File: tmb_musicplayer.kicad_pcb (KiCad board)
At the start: 2 copper layers, 99.1 x 95.3 mm, 138 parts, among them J1 Micro_SD, J2 RC522_Header, J3 Screw_Terminal_1x02, P1 SWD, P2 VolDown, P3 Prev, P4 Play, P5 Next, P6 VolUp, P7 CONN_02X10, Q1 BSS138, U1 VS1053, U2 STM32F407VGTx_minimal, U3 LD3985M18R, U4 LM22676QMRX-5.0, U5 LD3985M33R, U7 STEREO-AUDIO-JACK, Y1 12.288 Mhz, Y2 8MHz

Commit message: new layout
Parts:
- removed JP1, JP2: JUMPER, Capacitors_SMD:C_0603
- added C56: 1uF, Capacitors_SMD:C_0603, F.Cu at (64.4, 154.1)
- added C57: 100nF, Capacitors_SMD:C_0402, F.Cu at (62.5, 159.9)
- added C58: 10nF, Capacitors_SMD:C_0603, F.Cu at (66.4, 160.5)
- added C59: 1uF, Capacitors_SMD:C_0603, F.Cu at (68.8, 152.9)
- added C60: 100nF, Capacitors_SMD:C_0402, F.Cu at (78.4, 156.0)
- added R46: 0, Resistors_SMD:R_0603, F.Cu at (77.7, 159.9)
- added R47: 0, Resistors_SMD:R_0603, F.Cu at (73.9, 161.1)
- added R48: 0, Resistors_SMD:R_0603, F.Cu at (70.4, 160.5)
- added R49: 0, Resistors_SMD:R_0603, F.Cu at (75.2, 153.5)
- added U6: LD3985M33R, TO_SOT_Packages_SMD:SOT-23-5, F.Cu at (156.4, 144.0)
- added W10: SCLK, Measurement_Points:Measurement_Point_Round-SMD-Pad_Small, F.Cu at (70.7, 172.6)
- added W11: MCLK, Measurement_Points:Measurement_Point_Round-SMD-Pad_Small, F.Cu at (118.3, 167.5)
- added W12: XRESET, Measurement_Points:Measurement_Point_Round-SMD-Pad_Small, F.Cu at (129.1, 167.5)
- added W13: LROUT, Measurement_Points:Measurement_Point_Round-SMD-Pad_Small, F.Cu at (145.0, 169.4)
- added W14: LEDDIN, Measurement_Points:Measurement_Point_Round-SMD-Pad_Small, F.Cu at (97.4, 172.6)
- added W15: BTNDO, Measurement_Points:Measurement_Point_Round-SMD-Pad_Small, F.Cu at (134.8, 169.4)
- added W16: SDA, Measurement_Points:Measurement_Point_Round-SMD-Pad_Small, F.Cu at (155.2, 169.4)
- added W17: RESET, Measurement_Points:Measurement_Point_Round-SMD-Pad_Small, F.Cu at (77.7, 174.5)
- added W18: SCK, Measurement_Points:Measurement_Point_Round-SMD-Pad_Small, F.Cu at (91.7, 173.2)
- added W19: IRQ, Measurement_Points:Measurement_Point_Round-SMD-Pad_Small, F.Cu at (61.2, 172.6)
- added W20: MOSI, Measurement_Points:Measurement_Point_Round-SMD-Pad_Small, F.Cu at (50.4, 166.2)
- added W21: MISO, Measurement_Points:Measurement_Point_Round-SMD-Pad_Small, F.Cu at (46.0, 154.8)
- added W22: 3v3, Measurement_Points:Measurement_Point_Round-SMD-Pad_Small, F.Cu at (46.6, 159.9)
- added W23: BTNPR, Measurement_Points:Measurement_Point_Round-SMD-Pad_Small, F.Cu at (46.0, 144.0)
- added W24: BTNPL, Measurement_Points:Measurement_Point_Round-SMD-Pad_Small, F.Cu at (108.2, 158.6)
- added W25: D2, Measurement_Points:Measurement_Point_Round-SMD-Pad_Small, F.Cu at (58.0, 145.2)
- added W26: D1, Measurement_Points:Measurement_Point_Round-SMD-Pad_Small, F.Cu at (56.1, 151.6)
- added W27: 3V3, Measurement_Points:Measurement_Point_Round-SMD-Pad_Small, F.Cu at (55.5, 155.4)
- added W28: D0, Measurement_Points:Measurement_Point_Round-SMD-Pad_Small, F.Cu at (87.2, 159.2)
- added W29: D3, Measurement_Points:Measurement_Point_Round-SMD-Pad_Small, F.Cu at (68.2, 146.5)
- added W30: CD, Measurement_Points:Measurement_Point_Round-SMD-Pad_Small, F.Cu at (72.6, 149.1)
- added W31: CMD, Measurement_Points:Measurement_Point_Round-SMD-Pad_Small, F.Cu at (89.1, 151.0)
- added W32: BTNNE, Measurement_Points:Measurement_Point_Round-SMD-Pad_Small, F.Cu at (96.1, 155.4)
- added W33: SD_CD, Measurement_Points:Measurement_Point_Round-SMD-Pad_Small, F.Cu at (108.2, 174.5)
- added W34: BTNUP, Measurement_Points:Measurement_Point_Round-SMD-Pad_Small, F.Cu at (119.6, 177.0)
- added W35: 3.3V, Measurement_Points:Measurement_Point_Round-SMD-Pad_Small, F.Cu at (130.4, 175.1)
- added W36: 1V8, Measurement_Points:Measurement_Point_Round-SMD-Pad_Small, F.Cu at (49.1, 136.4)
- added W37: 3V3A, Measurement_Points:Measurement_Point_Round-SMD-Pad_Small, F.Cu at (54.2, 142.7)
- added W4: MISO, Measurement_Points:Measurement_Point_Round-SMD-Pad_Small, F.Cu at (103.1, 168.1)
- added W5: MOSI, Measurement_Points:Measurement_Point_Round-SMD-Pad_Small, F.Cu at (92.9, 167.5)
- added W6: SCLK, Measurement_Points:Measurement_Point_Round-SMD-Pad_Small, F.Cu at (110.7, 168.1)
- added W7: XCS, Measurement_Points:Measurement_Point_Round-SMD-Pad_Small, F.Cu at (87.9, 166.2)
- added W8: SDATA, Measurement_Points:Measurement_Point_Round-SMD-Pad_Small, F.Cu at (83.4, 171.9)
- added W9: XDCS, Measurement_Points:Measurement_Point_Round-SMD-Pad_Small, F.Cu at (77.7, 168.7)
- C1, C2, C24, C25: footprint Capacitors_SMD:C_0603_HandSoldering -> Capacitors_SMD:C_0603
- C26, C27: value 10uF -> 75uF
- C48: value CP -> 75uF; footprint Capacitors_THT:C_Radial_D5_L6_P2.5 -> Capacitors_SMD:c_elec_5x5.7
- D1: value CardDetect - Yellow -> LED_Yellow; footprint Capacitors_SMD:C_0603_HandSoldering -> Diodes_SMD:D_0603
- D2: value READ-Red -> LED_Red; footprint Capacitors_SMD:C_0603_HandSoldering -> Diodes_SMD:D_0603
- D3: value Decode - Green -> LED_Green; footprint Capacitors_SMD:C_0603_HandSoldering -> Diodes_SMD:D_0603
- D4: value RFIDDetect - Orange -> LED_Orange; footprint Capacitors_SMD:C_0603_HandSoldering -> Diodes_SMD:D_0603
- D5: value LED_Spare - Green -> LED_Green; footprint Capacitors_SMD:C_0603_HandSoldering -> Diodes_SMD:D_0603
- D6: value Heartbeat - Blue -> LED_Blue; footprint Capacitors_SMD:C_0603_HandSoldering -> Diodes_SMD:D_0603
- D7: value B560C-13-F -> D_Schottky_60V_5A
- D8: value D_Schottky -> D_Schottky_30_V_3A; footprint Diodes_SMD:SMB_Handsoldering -> Diodes_SMD:SMB_Standard
- L1: value 600R -> 10uH; footprint Resistors_SMD:R_0603 -> MF_Passives:MF_Passives-L1210
- L2: value 82uH -> 33uH
- R1, R10, R11, R12, R13, R14, R15, R16, R17, R18, R19, R2, R20, R21, R22, R23, R24, R25, R26, R27, R28, R29, R3, R30, R31, R32, R39, R4, R40, R41, R42, R43, R44, R45, R5, R6, R7, R8, R9: footprint Resistors_SMD:R_0603_HandSoldering -> Resistors_SMD:R_0603
- R36: footprint Resistors_SMD:R_0805_HandSoldering -> Resistors_SMD:R_0603
- R37, R38: footprint Capacitors_SMD:C_0603 -> Resistors_SMD:R_0603
- U2: value STM32F407VGTx_minimal -> STM32F407VGTx
- U7: value STEREO-AUDIO-JACK -> LINEOUT
- Y1, Y2: footprint Crystals:Crystal_HC49-U_Vertical -> Crystals:Crystal_SMD_ABM3B
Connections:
- net Net-(R40-Pad2) renamed /VS1053/RIGHT
- C17 pad 1: GND -> Net-(C17-Pad1)
- C17 pad 2: Net-(C17-Pad2) -> GND
- C48 pad 1: +5V -> /Externals/BTLED_NET_5V
- C6 pad 2: Net-(C6-Pad2) -> GND
- J1 pad 4: +3V3 -> Net-(J1-Pad4)
- J1 pad 6: +3V3 -> GND
- J2 pad 8: +3V3 -> Net-(J2-Pad8)
- P2 pad 2: +5V -> /Externals/BTLED_NET_5V
- P3 pad 2: +5V -> /Externals/BTLED_NET_5V
- P4 pad 2: +5V -> /Externals/BTLED_NET_5V
- P5 pad 2: +5V -> /Externals/BTLED_NET_5V
- P6 pad 2: +5V -> /Externals/BTLED_NET_5V
- Q1 pad 1: +3V3 -> Net-(Q1-Pad1)
- R14 pad 1: +3V3 -> Net-(Q1-Pad1)
- R15 pad 1: +3V3 -> Net-(Q1-Pad1)
- R16 pad 1: +3V3 -> Net-(J1-Pad4)
- R17 pad 1: +3V3 -> Net-(Q1-Pad1)
- R18 pad 1: +3V3 -> Net-(J1-Pad4)
- R19 pad 1: +3V3 -> Net-(J1-Pad4)
- R20 pad 1: +3V3 -> Net-(J1-Pad4)
- R21 pad 1: +3V3 -> Net-(J1-Pad4)
- R22 pad 1: +3V3 -> Net-(J1-Pad4)
- R23 pad 1: +3V3 -> Net-(Q1-Pad1)
- R24 pad 1: +3V3 -> Net-(Q1-Pad1)
- R25 pad 1: +5V -> /Externals/BTLED_NET_5V
- R31 pad 1: +3V3 -> Net-(J1-Pad4)
- R32 pad 1: +3V3 -> Net-(Q1-Pad1)
- R34 pad 2: +3V3 -> +3.3VA
- R41 pad 2: Net-(R41-Pad2) -> /VS1053/LEFT
- R6 pad 1: Net-(C17-Pad2) -> /VS1053/LEFT
- R6 pad 2: Net-(R41-Pad2) -> Net-(C17-Pad1)
- U1 pad 10: /VS1053/SDA -> Net-(R3-Pad1)
- U1 pad 46: Net-(R41-Pad2) -> /VS1053/LEFT
- U1 pad 9: /VS1053/SCL -> Net-(R3-Pad1)
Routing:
- net +3V3: track 354.7 -> 176.8 mm, vias 8 -> 3
- net GND: track 781.0 -> 924.7 mm, vias 66 -> 71
- net +5V: track 183.6 -> 134.1 mm
- net /Externals/BTLED_NET_5V: track 0.00 -> 49.5 mm
- net /VS1053/SDA: track 48.4 -> 0.00 mm, vias 4 -> 0
- net /VS1053/SCL: track 48.4 -> 0.00 mm, vias 2 -> 0
- net Net-(J1-Pad4): track 0.00 -> 18.6 mm
- net Net-(R41-Pad2): track 11.5 -> 0.00 mm
- net /VS1053/LEFT: track 0.00 -> 11.5 mm
- net VDD: track 134.3 -> 125.4 mm
- net /Main/VDDA: track 17.1 -> 26.0 mm
- net /PB7: track 122.8 -> 114.9 mm
- net /PB6: track 116.0 -> 108.4 mm
- net Net-(R3-Pad1): track 6.11 -> 13.0 mm, vias 0 -> 2
- net Net-(C17-Pad1): track 0.00 -> 5.06 mm
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
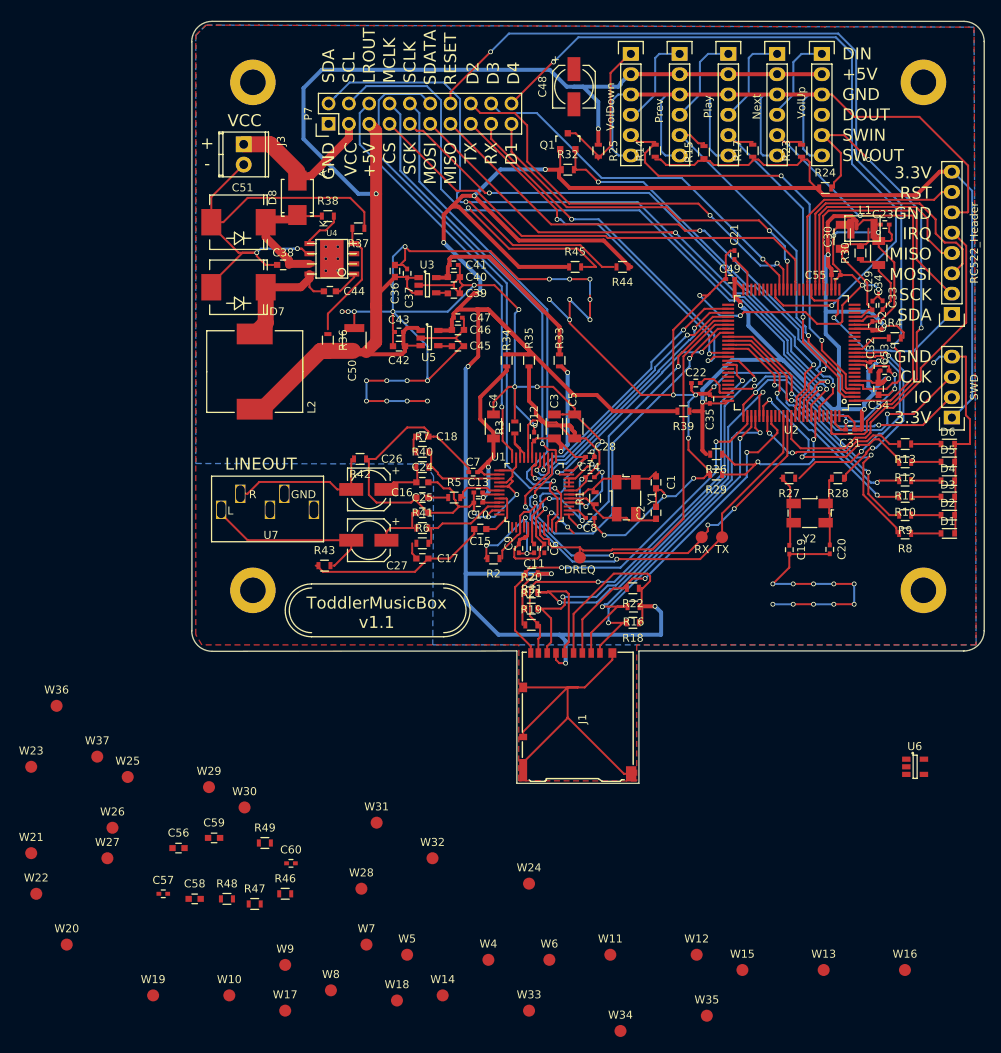
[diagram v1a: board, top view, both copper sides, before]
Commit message: Macrofab sd card footprint
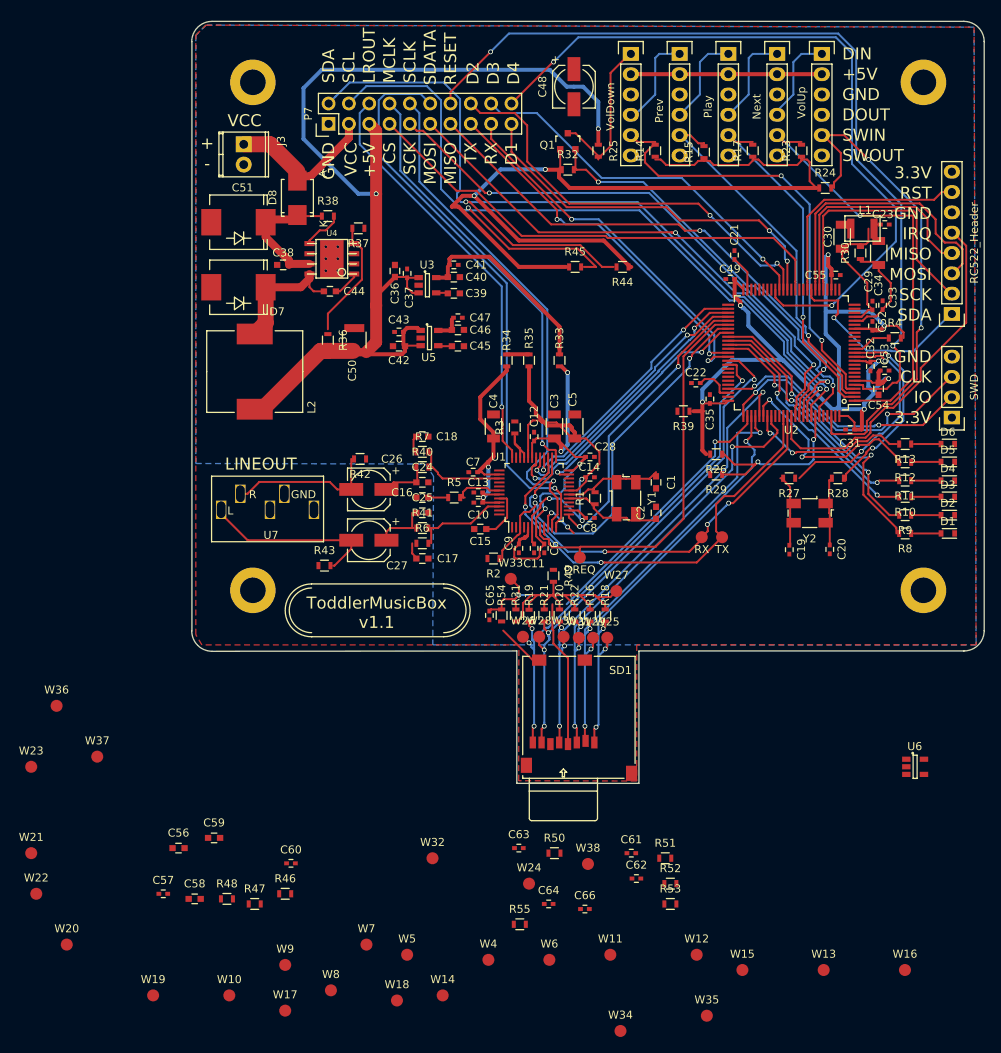
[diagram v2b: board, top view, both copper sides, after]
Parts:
- removed J1: Micro_SD, conn-io:HIROSE-MICROSD-DM3AT-SF
- added C61: 100nF, Capacitors_SMD:C_0402, F.Cu at (121.0, 154.8)
- added C62: 100nF, Capacitors_SMD:C_0402, F.Cu at (121.6, 157.9)
- added C63: 100nF, Capacitors_SMD:C_0402, F.Cu at (106.9, 154.1)
- added C64: 100nF, Capacitors_SMD:C_0402, F.Cu at (110.6, 161.1)
- added C65: 100nF, Capacitors_SMD:C_0402, F.Cu at (103.2, 125.1)
- added C66: 100nF, Capacitors_SMD:C_0402, F.Cu at (115.2, 161.8)
- added R50: 1k, Resistors_SMD:R_0603, F.Cu at (111.4, 154.8)
- added R51: 1k, Resistors_SMD:R_0603, F.Cu at (125.2, 155.4)
- added R52: 1k, Resistors_SMD:R_0603, F.Cu at (125.8, 158.6)
- added R53: 1k, Resistors_SMD:R_0603, F.Cu at (125.8, 161.1)
- added R54: 1k, Resistors_SMD:R_0603, F.Cu at (104.8, 125.1)
- added R55: 1k, Resistors_SMD:R_0603, F.Cu at (107.0, 163.7)
- added SD1: MICROSD_CARD_RIGHT, MF_Connectors:MF_Connectors-MF-MICROSD, F.Cu at (114.4, 137.8)
- added W38: 3V3A, Measurement_Points:Measurement_Point_Round-SMD-Pad_Small, F.Cu at (115.5, 156.1)
- moved W27 71.9 mm to (119.1, 122.0)
- moved W25 62.4 mm to (118.0, 127.9)
- moved W26 56.6 mm to (107.4, 127.7)
- moved W33 54.0 mm to (105.9, 120.5)
- moved W29 51.5 mm to (116.2, 127.9)
- moved R49 49.2 mm to (111.2, 120.1), turned to 270 degrees
- moved W30 45.2 mm to (112.5, 127.7)
- moved W28 38.5 mm to (109.5, 127.7)
- moved W31 34.2 mm to (114.4, 127.9)
- moved R22 8.02 mm to (113.9, 125.1), turned to 270 degrees
- moved R31 5.57 mm to (106.5, 125.1), turned to 90 degrees
- moved R16 5.55 mm to (115.8, 125.1), turned to 270 degrees
- moved R20 4.56 mm to (112.0, 125.1), turned to 270 degrees
- moved R18 3.58 mm to (117.7, 125.1), turned to 270 degrees
- moved R21 1.84 mm to (110.1, 125.1), turned to 270 degrees
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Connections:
- P2 pad 5: /PE5 -> Net-(P2-Pad5)
- P3 pad 5: /PE4 -> Net-(P3-Pad5)
- P4 pad 5: /PE3 -> Net-(P4-Pad5)
- P5 pad 5: /PE2 -> Net-(P5-Pad5)
- P6 pad 5: /PE1 -> Net-(P6-Pad5)
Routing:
- net GND: track 924.7 -> 2.17 mm, vias 71 -> 0
- net +3V3: track 176.8 -> 118.0 mm, vias 3 -> 2
- net /PE1: track 62.2 -> 22.7 mm, vias 2 -> 0
- net Net-(P6-Pad5): track 0.00 -> 39.5 mm, vias 0 -> 2
- net Net-(P3-Pad5): track 0.00 -> 32.8 mm
- net /PE4: track 45.8 -> 13.0 mm
- net Net-(R16-Pad1): track 18.6 -> 49.2 mm
- net Net-(P4-Pad5): track 0.00 -> 30.3 mm
- net /PE3: track 43.6 -> 13.4 mm
- net Net-(P5-Pad5): track 0.00 -> 18.5 mm, vias 0 -> 1
- net /PE2: track 53.5 -> 35.0 mm, vias 1 -> 0
- net /PD2: track 42.6 -> 58.4 mm, vias 2 -> 4
- net /PC10: track 40.3 -> 54.5 mm, vias 2 -> 4
- net /PC11: track 45.0 -> 56.1 mm, vias 2 -> 4
- net /PC8: track 55.5 -> 65.6 mm, vias 2 -> 4
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
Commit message: Finished new layout
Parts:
- removed C53, C55: 100nF, Capacitors_SMD:C_0402
- added R56: 100k, Resistors_SMD:R_0603, F.Cu at (116.6, 115.4)
- moved W22 135.7 mm to (152.8, 75.3)
- moved W20 124.7 mm to (143.1, 82.8)
- moved W21 122.3 mm to (142.9, 80.2)
- moved R48 117.9 mm to (150.5, 73.9)
- moved W17 117.5 mm to (141.2, 75.7)
- moved W34 109.8 mm to (145.0, 70.2)
- moved W23 109.8 mm to (127.2, 70.2)
- moved W19 108.3 mm to (147.3, 106.9)
- moved W18 106.7 mm to (157.8, 89.5)
- moved R55 105.9 mm to (147.4, 65.7), turned to 270 degrees
- moved W14 104.7 mm to (116.1, 69.6)
- moved W15 100.3 mm to (120.9, 70.1)
- moved C66 99.6 mm to (147.9, 67.7)
- moved C64 98.6 mm to (142.0, 67.7)
- moved W35 98.5 mm to (101.4, 81.0)
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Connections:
- U1 pad 10: Net-(R3-Pad1) -> Net-(R56-Pad1)
- U1 pad 9: Net-(R3-Pad1) -> Net-(R56-Pad1)
- U4 pad 9: (no net) -> GND
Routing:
- net GND: track 2.17 -> 799.8 mm, vias 0 -> 138
- net +3V3: track 118.0 -> 196.0 mm, vias 2 -> 8
- net Net-(Q1-Pad1): track 2.92 -> 76.4 mm, vias 0 -> 6
- net /PE11: track 92.4 -> 37.5 mm, vias 2 -> 1
- net /Externals/BTLED_NET_5V: track 41.8 -> 92.5 mm
- net /PE6: track 106.8 -> 63.2 mm
- net Net-(P6-Pad5): track 39.5 -> 2.60 mm, vias 2 -> 0
- net Net-(P3-Pad5): track 32.8 -> 2.96 mm
- net /PE4: track 13.0 -> 42.3 mm, vias 1 -> 2
- net /PE3: track 13.4 -> 41.5 mm, vias 1 -> 2
- net Net-(P4-Pad5): track 30.3 -> 2.40 mm
- net /PB7: track 114.9 -> 90.0 mm, vias 2 -> 1
- net /PD5: track 56.4 -> 33.4 mm, vias 2 -> 4
- net Net-(R27-Pad1): track 27.9 -> 5.05 mm, vias 2 -> 0
- net /PB6: track 108.4 -> 87.1 mm, vias 2 -> 1
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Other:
- board text removed: "DREQ"

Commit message: increased Version
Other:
- board text added: "ToddlerMusicBox v1.2"
- board text removed: "ToddlerMusicBox v1.1"
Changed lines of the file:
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@@
     (effects (font (size 1.5 1.5) (thickness 0.3)) (justify left))
   )
-  (gr_text "ToddlerMusicBox\nv1.1" (at 89.13 124.714) (layer F.SilkS)
+  (gr_text "ToddlerMusicBox\nv1.2" (at 89.13 124.714) (layer F.SilkS)
     (effects (font (size 1.5 1.5) (thickness 0.3)))
   )
